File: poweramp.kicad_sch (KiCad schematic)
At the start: 84 parts, among them IC1 TPA3255, U2 Opamp_Dual

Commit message: update partnumbers to what was bought
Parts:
- U2: value Opamp_Dual -> (undecided)
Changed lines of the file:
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@@
 			)
 		)
-		(property "Value" "Opamp_Dual"
+		(property "Value" "(undecided)"
 			(at 143.51 176.53 0)
 			(effects
@@
 			)
 		)
-		(property "Value" "Opamp_Dual"
+		(property "Value" "(undecided)"
 			(at 152.4 143.51 0)
 			(effects
@@
 			)
 		)
-		(property "Value" "Opamp_Dual"
+		(property "Value" "(undecided)"
 			(at 193.04 156.845 0)
 			(effects

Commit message: print cheatsheets
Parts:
- JP1: value SolderJumper_3_Bridged12 -> M2
- JP2: value SolderJumper_3_Bridged12 -> M1
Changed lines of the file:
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@@
 			)
 		)
-		(property "Value" "SolderJumper_3_Bridged12"
+		(property "Value" "M2"
 			(at 88.9 78.105 90)
 			(effects
@@
 			)
 		)
-		(property "Value" "SolderJumper_3_Bridged12"
+		(property "Value" "M1"
 			(at 81.28 80.645 90)
 			(effects

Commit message: workaround major gain/signal margin error
using the components i have at hand. There probably are better options. Next revision should make use of the -5v rail.
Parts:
- R11, R12, R13, R14: value 330 -> t330
- R15, R16, R17, R18: value 10k -> t10k
- U2: value (undecided) -> OPA1642
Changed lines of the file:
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@@
 			)
 		)
-		(property "Value" "(undecided)"
+		(property "Value" "OPA1642"
 			(at 143.51 176.53 0)
 			(effects
@@
 			)
 		)
-		(property "Value" "10k"
+		(property "Value" "t10k"
 			(at 41.91 168.91 90)
 			(effects
@@
 			)
 		)
-		(property "Value" "10k"
+		(property "Value" "t10k"
 			(at 87.63 168.91 90)
 			(effects
@@
 			)
 		)
-		(property "Value" "10k"
+		(property "Value" "t10k"
 			(at 87.63 181.61 90)
 			(effects
@@
 			)
 		)
-		(property "Value" "330"
+		(property "Value" "t330"
 			(at 69.85 162.56 90)
 			(effects
@@
 			)
 		)
-		(property "Value" "(undecided)"
+		(property "Value" "OPA1642"
 			(at 152.4 143.51 0)
 			(effects
@@
 			)
 		)
-		(property "Value" "(undecided)"
+		(property "Value" "OPA1642"
 			(at 193.04 156.845 0)
 			(effects
@@
 			)
 		)
-		(property "Value" "330"
+		(property "Value" "t330"
 			(at 69.85 175.26 90)
 			(effects
@@
 			)
 		)
-		(property "Value" "330"
+		(property "Value" "t330"
 			(at 24.13 175.26 90)
 			(effects
@@
 			)
 		)
-		(property "Value" "10k"
+		(property "Value" "t10k"
 			(at 41.91 181.61 90)
 			(effects
@@
 			)
 		)
-		(property "Value" "330"
+		(property "Value" "t330"
 			(at 24.13 162.56 90)
 			(effects

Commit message: work on bugs...
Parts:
- removed C4: 100p, invendelirium_audio:C_0603, symbol Device:C
- removed R10: 100, invendelirium_audio:R_0603, symbol Device:R_Small
- C14, C3: value 1u -> 10u
- R9: value 47k -> 10k
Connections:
- net GND: no longer C9.2
- net input_ref: now also C9.1
- net ~reset: now also IC1.18 (18_RESET), R9.1
- net at R19.1, U2.3 (+): now also C9.2; no longer C9.1
- net c_start: now reaches C12.1, IC1.15 (15_C_START)
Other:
- moved on the sheet: C12, C14, C9, JP3, R24, R25, R9, s30

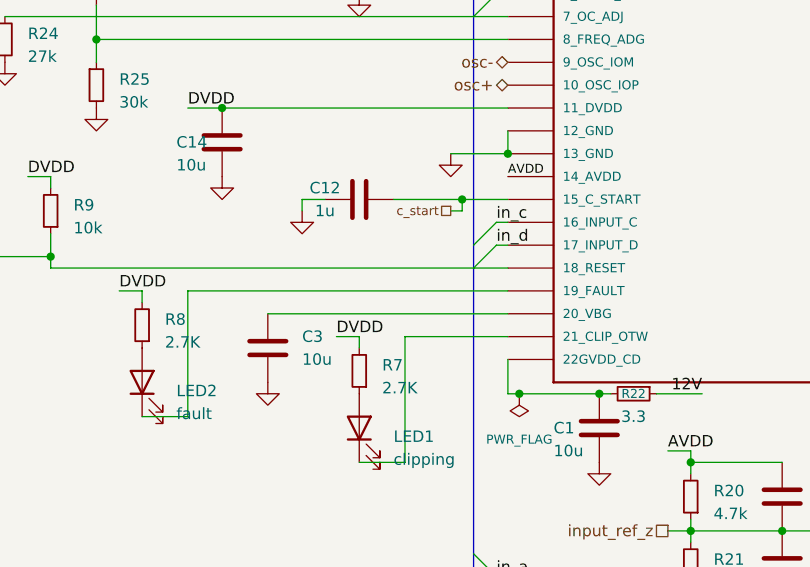
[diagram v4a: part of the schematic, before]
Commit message: work on bugs
* align parts
* enlarge cercaps
* fix ak caps
* improve jack footprint
* fix lmr stencil openings
* remove one ldo
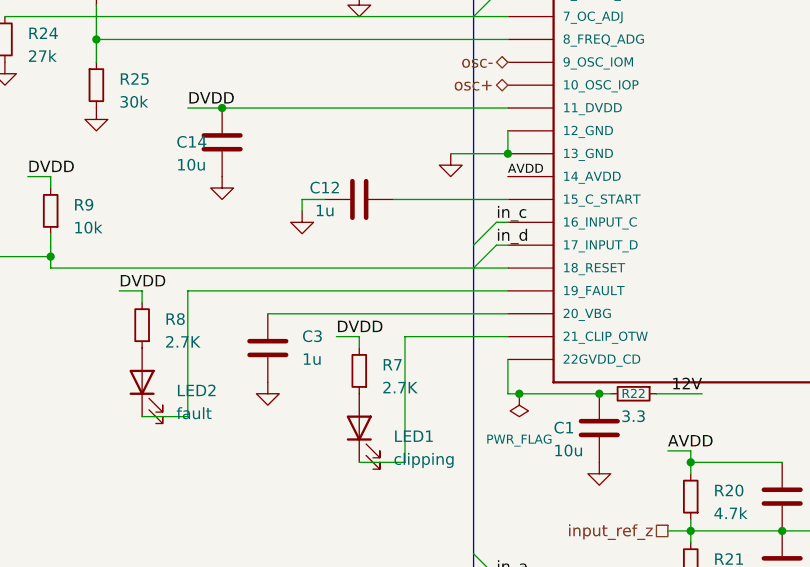
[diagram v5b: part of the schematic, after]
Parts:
- C1, C13, C14, C15, C16, C17, C18, C2, CR0, CU2: footprint invendelirium_audio:C_0603 -> invendelirium_audio:C_0603_larger
- C3: value 10u -> 1u
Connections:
- net c_start: no longer names the net of C12.1, IC1.15 (15_C_START)
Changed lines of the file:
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@@
 	)
 	(junction
-		(at 99.06 110.49)
-		(diameter 0)
-		(color 0 0 0 0)
-	)
-	(junction
 		(at 215.9 110.49)
 		(diameter 0)
@@
 	(wire
 		(pts
-			(xy 99.06 111.76) (xy 99.06 110.49)
-		)
-		(stroke
-			(width 0)
-			(type default)
-		)
-	)
-	(wire
-		(pts
 			(xy 26.67 177.8) (xy 30.48 177.8)
 		)
@@
 	(wire
 		(pts
-			(xy 99.06 110.49) (xy 104.14 110.49)
-		)
-		(stroke
-			(width 0)
-			(type default)
-		)
-	)
-	(wire
-		(pts
 			(xy 215.9 76.2) (xy 233.68 76.2)
 		)
@@
 	(wire
 		(pts
-			(xy 91.44 110.49) (xy 99.06 110.49)
+			(xy 91.44 110.49) (xy 104.14 110.49)
 		)
 		(stroke
@@
 	(wire
 		(pts
-			(xy 77.47 123.19) (xy 104.14 123.19)
-		)
-		(stroke
-			(width 0)
-			(type default)
-		)
-	)
-	(wire
-		(pts
 			(xy 181.61 67.31) (xy 185.42 67.31)
 		)
@@
 	(wire
 		(pts
+			(xy 77.47 123.19) (xy 104.14 123.19)
+		)
+		(stroke
+			(width 0)
+			(type default)
+		)
+	)
+	(wire
+		(pts
 			(xy 196.85 110.49) (xy 194.31 110.49)
 		)
@@
 	(wire
 		(pts
-			(xy 97.79 111.76) (xy 99.06 111.76)
-		)
-		(stroke
-			(width 0)
-			(type default)
-		)
-	)
-	(wire
-		(pts
 			(xy 48.26 90.17) (xy 100.33 90.17)
 		)
@@
 		)
 	)
-	(hierarchical_label "c_start"
-		(shape passive)
-		(at 97.79 111.76 180)
-		(fields_autoplaced yes)
-		(effects
-			(font
-				(size 1.016 1.016)
-			)
-			(justify right)
-		)
-	)
 	(hierarchical_label "in2"
 		(shape input)
@@
 			)
 		)
-		(property "Footprint" "invendelirium_audio:C_0603"
+		(property "Footprint" "invendelirium_audio:C_0603_larger"
 			(at 167.3352 157.48 0)
 			(effects
@@
 			)
 		)
-		(property "Footprint" "invendelirium_audio:C_0603"
+		(property "Footprint" "invendelirium_audio:C_0603_larger"
 			(at 73.3552 107.95 0)
 			(effects
@@
 			)
 		)
-		(property "Footprint" "invendelirium_audio:C_0603"
+		(property "Footprint" "invendelirium_audio:C_0603_larger"
 			(at 211.7852 158.75 0)
 			(effects
@@
 			)
 		)
-		(property "Value" "10u"
+		(property "Value" "1u"
 			(at 81.28 128.2699 0)
 			(effects
@@
 			)
 		)
-		(property "Footprint" "invendelirium_audio:C_0603"
+		(property "Footprint" "invendelirium_audio:C_0603_larger"
 			(at 90.4748 54.61 0)
 			(effects
@@
 			)
 		)
-		(property "Footprint" "invendelirium_audio:C_0603"
+		(property "Footprint" "invendelirium_audio:C_0603_larger"
 			(at 52.07 176.8348 0)
 			(effects
@@
 			)
 		)
-		(property "Footprint" "invendelirium_audio:C_0603"
+		(property "Footprint" "invendelirium_audio:C_0603_larger"
 			(at 115.2652 139.7 0)
 			(effects
@@
 			)
 		)
-		(property "Footprint" "invendelirium_audio:C_0603"
+		(property "Footprint" "invendelirium_audio:C_0603_larger"
 			(at 50.8 164.1348 0)
 			(effects
@@
 			)
 		)
-		(property "Footprint" "invendelirium_audio:C_0603"
+		(property "Footprint" "invendelirium_audio:C_0603_larger"
 			(at 97.79 176.8348 0)
 			(effects
@@
 			)
 		)
-		(property "Footprint" "invendelirium_audio:C_0603"
+		(property "Footprint" "invendelirium_audio:C_0603_larger"
 			(at 97.79 164.1348 0)
 			(effects
@@
 			)
 		)
-		(property "Footprint" "invendelirium_audio:C_0603"
+		(property "Footprint" "invendelirium_audio:C_0603_larger"
 			(at 115.57 61.2648 0)
 			(effects

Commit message: remove duplicate dac supply
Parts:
- C10, C11: footprint invendelirium_audio:C_0603 -> invendelirium_audio:C_0603_larger
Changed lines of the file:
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@@
 			)
 		)
-		(property "Footprint" "invendelirium_audio:C_0603"
+		(property "Footprint" "invendelirium_audio:C_0603_larger"
 			(at 135.5852 147.32 0)
 			(effects
@@
 			)
 		)
-		(property "Footprint" "invendelirium_audio:C_0603"
+		(property "Footprint" "invendelirium_audio:C_0603_larger"
 			(at 135.5852 154.94 0)
 			(effects

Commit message: all known bugs fixed
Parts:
- TP1: value out3 -> out0; footprint TestPoint:TestPoint_Pad_D4.0mm -> invendelirium_audio:output_pad
- TP2: value out2 -> out1; footprint TestPoint:TestPoint_Pad_D4.0mm -> invendelirium_audio:output_pad
- TP3: value out1 -> out2; footprint TestPoint:TestPoint_Pad_D4.0mm -> invendelirium_audio:output_pad
- TP4: value out0 -> out3; footprint TestPoint:TestPoint_Pad_D4.0mm -> invendelirium_audio:output_pad
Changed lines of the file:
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@@
 		(fields_autoplaced yes)
 		(property "Reference" "TP4"
-			(at 255.27 122.555 90)
+			(at 255.27 121.9199 90)
 			(effects
 				(font
@@
 			)
 		)
-		(property "Value" "out0"
-			(at 255.27 125.095 90)
+		(property "Value" "out3"
+			(at 255.27 124.4599 90)
 			(effects
 				(font
@@
 			)
 		)
-		(property "Footprint" "TestPoint:TestPoint_Pad_D4.0mm"
+		(property "Footprint" "invendelirium_audio:output_pad"
 			(at 250.19 128.27 0)
 			(effects
@@
 		(fields_autoplaced yes)
 		(property "Reference" "TP2"
-			(at 256.54 92.075 90)
+			(at 256.54 91.4399 90)
 			(effects
 				(font
@@
 			)
 		)
-		(property "Value" "out2"
-			(at 256.54 94.615 90)
+		(property "Value" "out1"
+			(at 256.54 93.9799 90)
 			(effects
 				(font
@@
 			)
 		)
-		(property "Footprint" "TestPoint:TestPoint_Pad_D4.0mm"
+		(property "Footprint" "invendelirium_audio:output_pad"
 			(at 251.46 97.79 0)
 			(effects
@@
 		(fields_autoplaced yes)
 		(property "Reference" "TP3"
-			(at 256.54 109.855 90)
+			(at 256.54 109.2199 90)
 			(effects
 				(font
@@
 			)
 		)
-		(property "Value" "out1"
-			(at 256.54 112.395 90)
+		(property "Value" "out2"
+			(at 256.54 111.7599 90)
 			(effects
 				(font
@@
 			)
 		)
-		(property "Footprint" "TestPoint:TestPoint_Pad_D4.0mm"
+		(property "Footprint" "invendelirium_audio:output_pad"
 			(at 251.46 115.57 0)
 			(effects
@@
 		(fields_autoplaced yes)
 		(property "Reference" "TP1"
-			(at 255.27 75.565 90)
+			(at 255.27 74.9299 90)
 			(effects
 				(font
@@
 			)
 		)
-		(property "Value" "out3"
-			(at 255.27 78.105 90)
+		(property "Value" "out0"
+			(at 255.27 77.4699 90)
 			(effects
 				(font
@@
 			)
 		)
-		(property "Footprint" "TestPoint:TestPoint_Pad_D4.0mm"
+		(property "Footprint" "invendelirium_audio:output_pad"
 			(at 250.19 81.28 0)
 			(effects

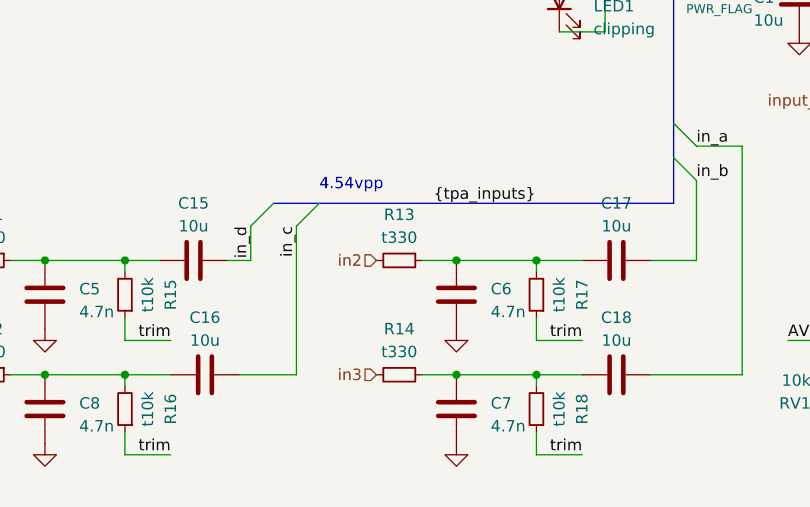
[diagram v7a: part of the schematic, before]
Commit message: updates for better bom
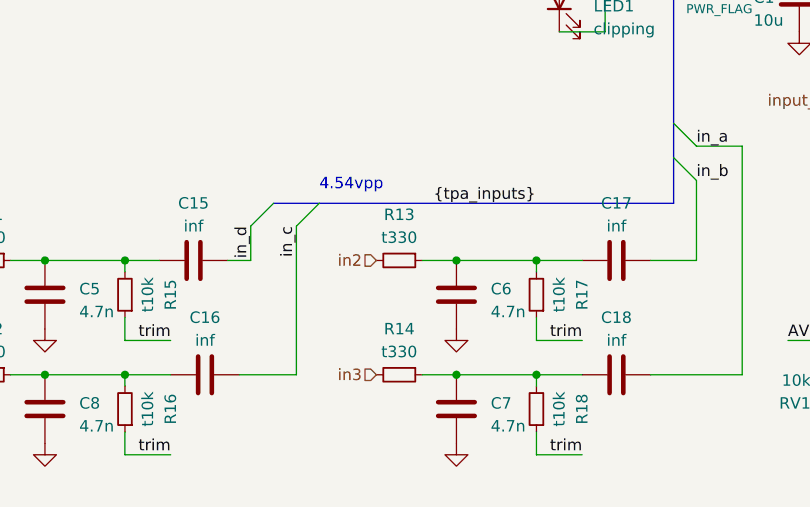
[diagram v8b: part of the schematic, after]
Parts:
- C15, C16, C17, C18: value 10u -> inf; now left out of the parts list
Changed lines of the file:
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@@
 		(unit 1)
 		(exclude_from_sim no)
-		(in_bom yes)
+		(in_bom no)
 		(on_board yes)
 		(dnp no)
@@
 			)
 		)
-		(property "Value" "10u"
+		(property "Value" "inf"
 			(at 48.26 173.99 90)
 			(effects
@@
 		(unit 1)
 		(exclude_from_sim no)
-		(in_bom yes)
+		(in_bom no)
 		(on_board yes)
 		(dnp no)
@@
 			)
 		)
-		(property "Value" "10u"
+		(property "Value" "inf"
 			(at 46.99 161.29 90)
 			(effects
@@
 		(unit 1)
 		(exclude_from_sim no)
-		(in_bom yes)
+		(in_bom no)
 		(on_board yes)
 		(dnp no)
@@
 			)
 		)
-		(property "Value" "10u"
+		(property "Value" "inf"
 			(at 93.98 173.99 90)
 			(effects
@@
 		(unit 1)
 		(exclude_from_sim no)
-		(in_bom yes)
+		(in_bom no)
 		(on_board yes)
 		(dnp no)
@@
 			)
 		)
-		(property "Value" "10u"
+		(property "Value" "inf"
 			(at 93.98 161.29 90)
 			(effects
